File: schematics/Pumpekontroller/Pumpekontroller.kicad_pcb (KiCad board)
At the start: 2 copper layers, 129.5 x 85.1 mm, 25 parts, among them K1 SRD-05VDC-SL-C, M1 Motor_DC, Q1 BC547, Q2 BC547, Q3 BC547, SW1 SW_Push, SW2 SW_Push, U1 WeMos_D1_mini

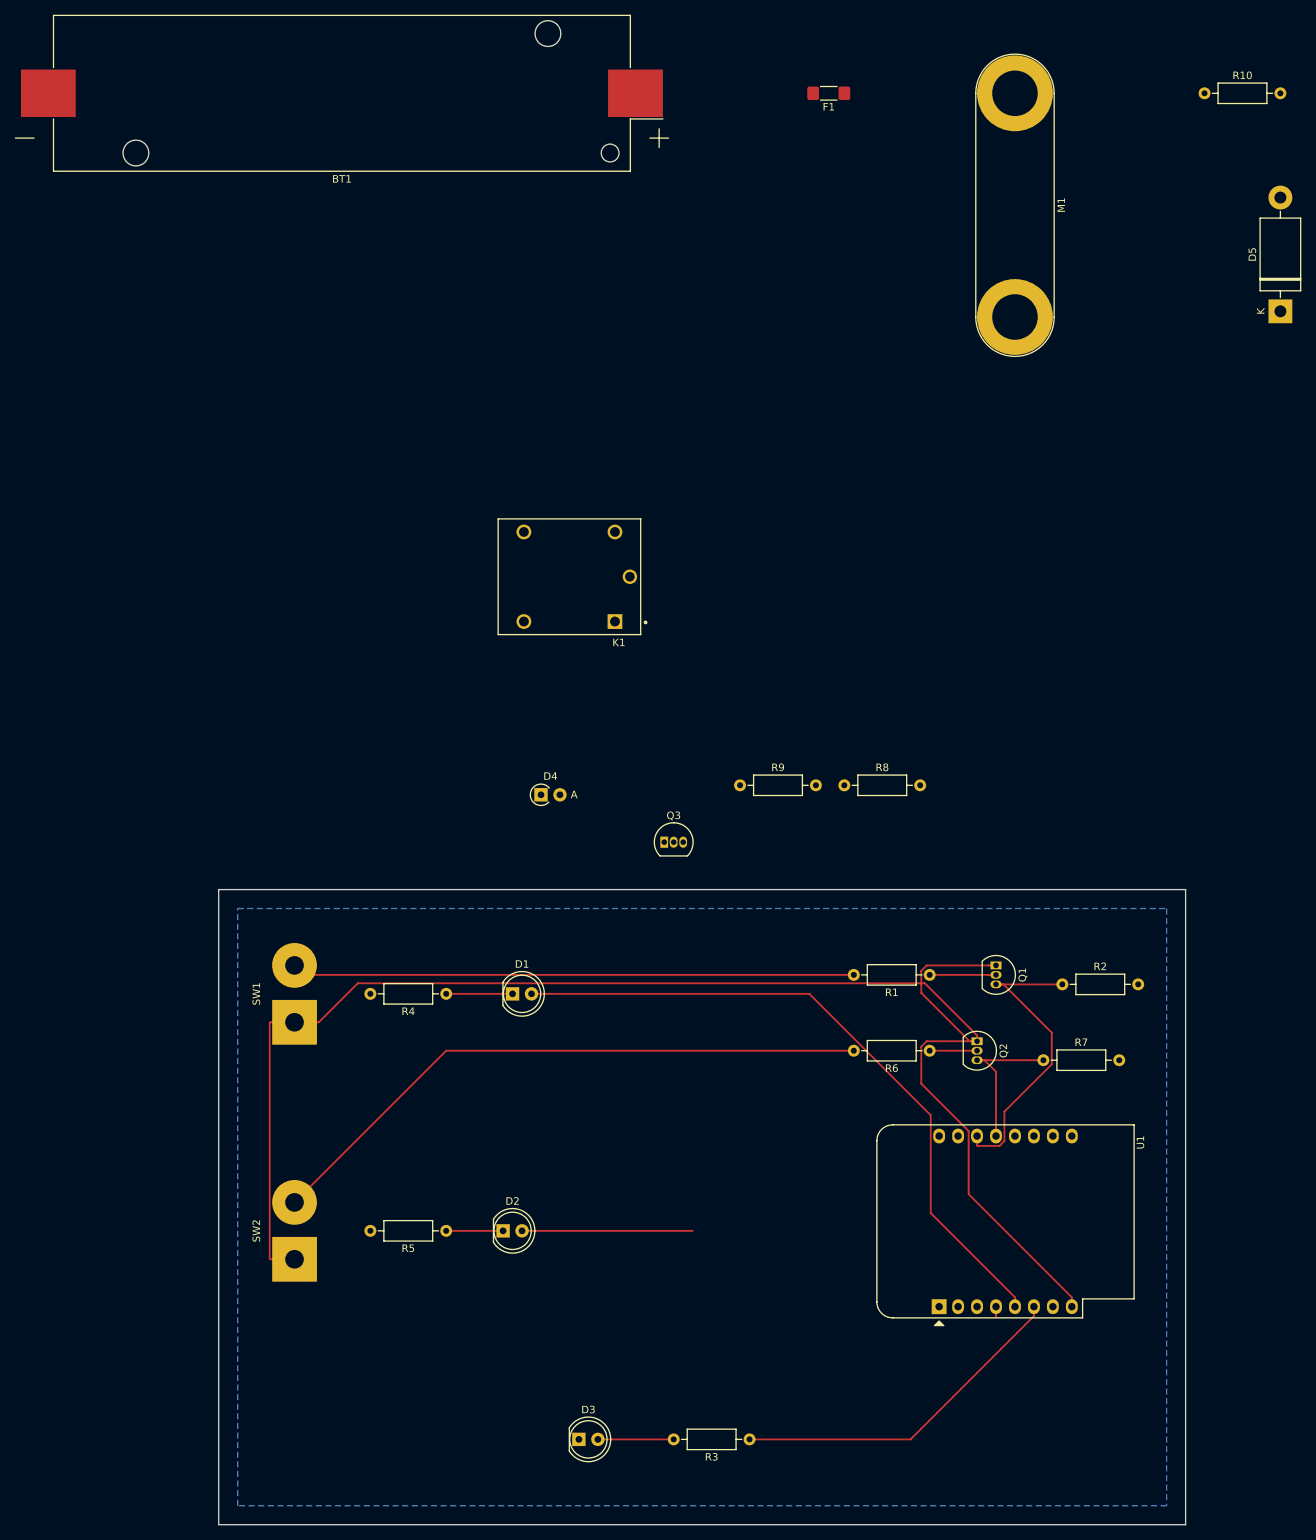
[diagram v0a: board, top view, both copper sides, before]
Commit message: Separate schema for pump controller and 12V pump circuit.
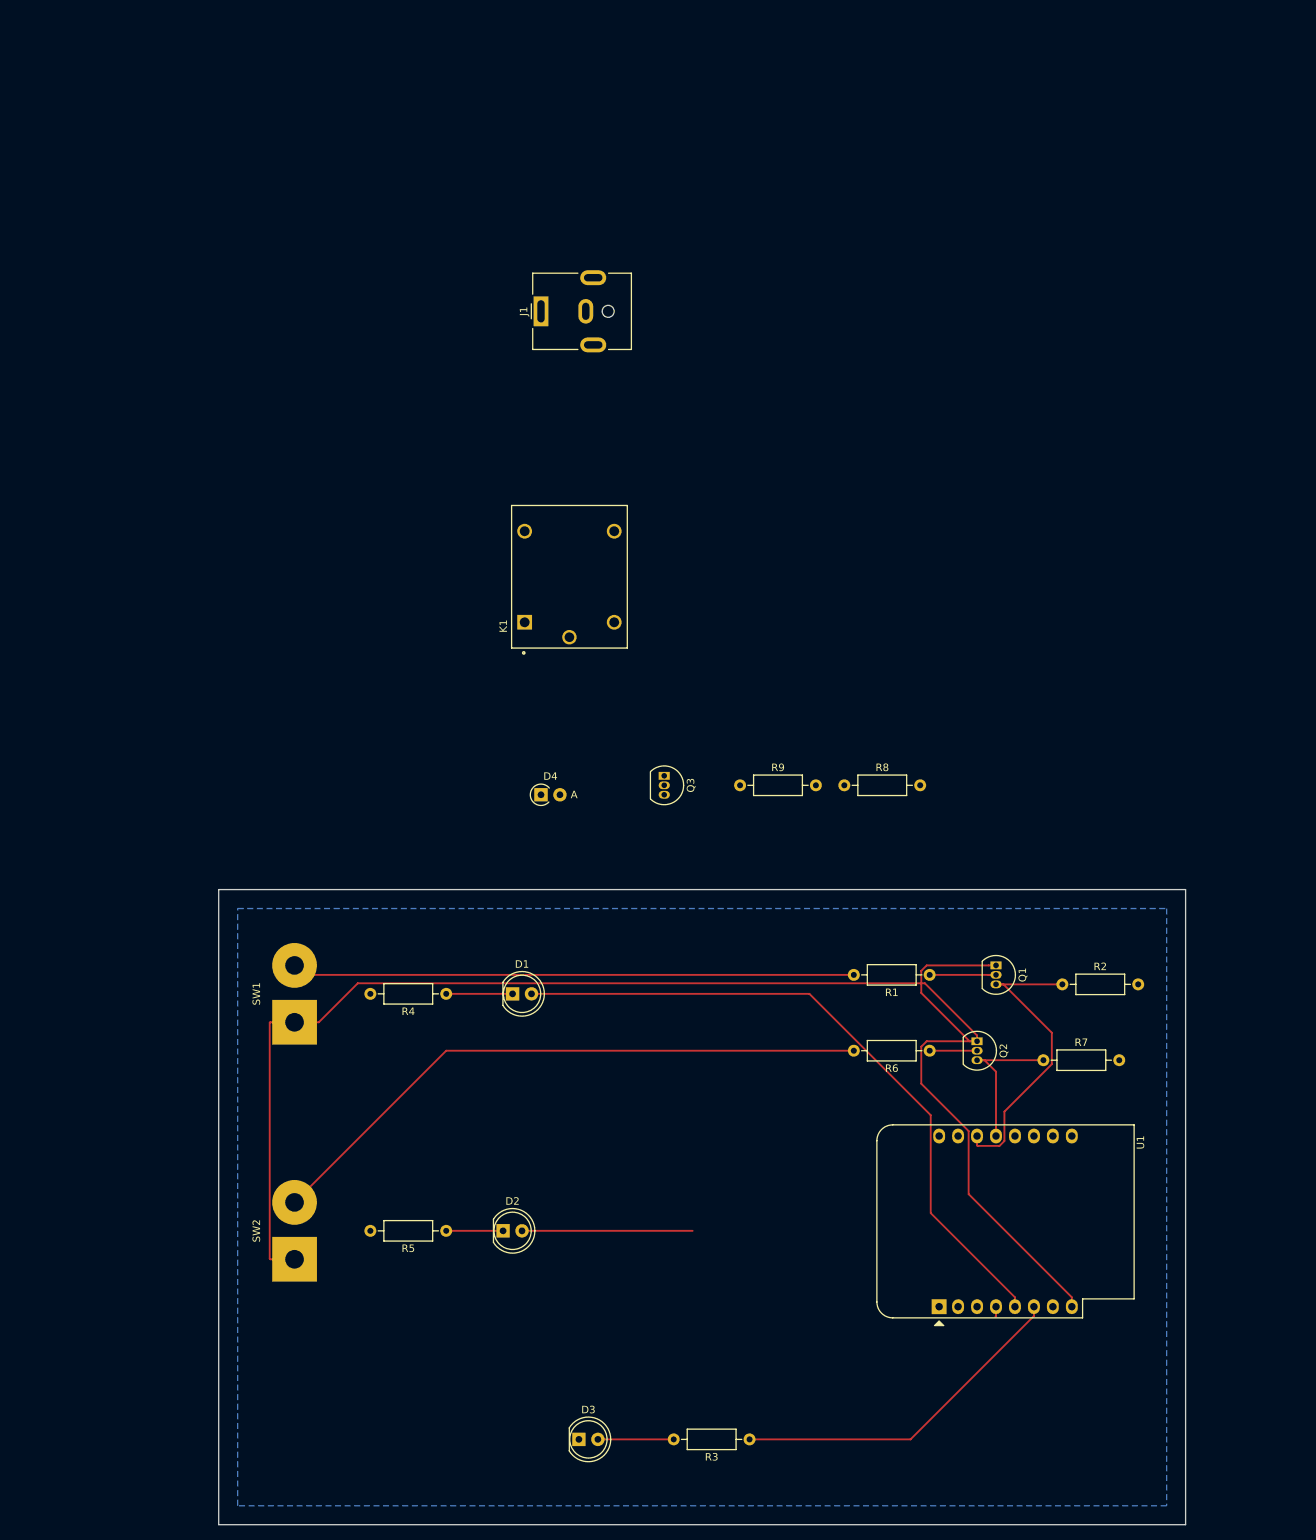
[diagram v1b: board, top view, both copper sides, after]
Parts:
- removed BT1: Battery 12V, Battery:BatteryHolder_Keystone_1042_1x18650
- removed D5: LED, Diode_THT:D_DO-201AD_P15.24mm_Horizontal
- removed F1: Fuse, Fuse:Fuse_1806_4516Metric_Pad1.57x1.80mm_HandSolder
- removed M1: Motor_DC, Connector:Banana_Jack_2Pin
- removed R10: 2.2kΩ, Resistor_THT:R_Axial_DIN0207_L6.3mm_D2.5mm_P10.16mm_Horizontal
- added J1: Barrel_Jack, Connector_BarrelJack:BarrelJack_CUI_PJ-063AH_Horizontal, F.Cu at (125.7, -25.4)
- moved Q3 8.89 mm to (142.2, 36.8), turned to 270 degrees
- turned K1 to 90 degrees
